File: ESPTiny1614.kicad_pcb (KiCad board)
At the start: 2 copper layers, 33 x 23.9 mm, 22 parts, among them J1 Conn_01x10_Male, J2 Conn_01x10_Male, J3 Conn_01x04_Male, U1 ESP-01v090, U2 ATtiny1614-SS, U3 MCP1700-3302E_TO92

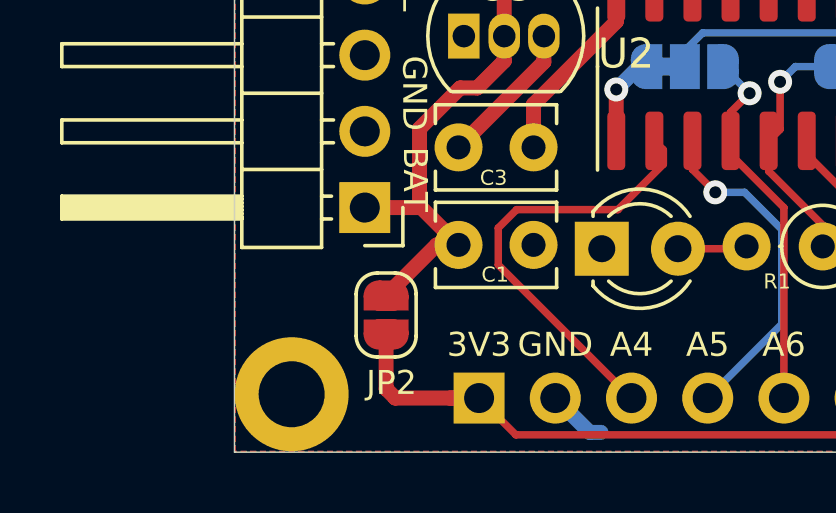
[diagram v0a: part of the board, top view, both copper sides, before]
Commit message: Change solder jumper footprint with thermal insulation
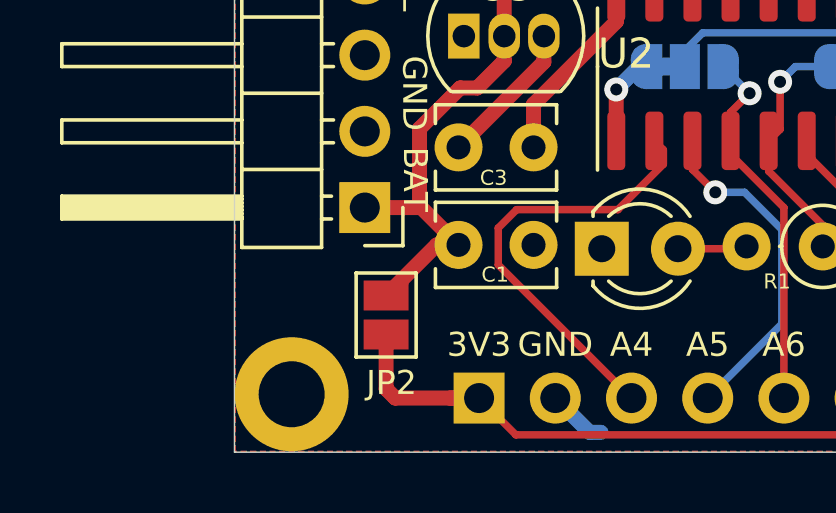
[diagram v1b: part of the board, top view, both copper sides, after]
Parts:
- JP2: footprint Jumper:SolderJumper-2_P1.3mm_Open_RoundedPad1.0x1.5mm -> Jumper:SolderJumper-2_P1.3mm_Open_Pad1.0x1.5mm

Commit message: Fix RST to A1
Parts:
- moved JP1 2.18 mm to (61.7, 51.6)
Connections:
- JP1 pad 1: /A7 -> /A1
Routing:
- net /A1: track 7.66 -> 14.8 mm, vias 0 -> 1
- net /RST: track 17.4 -> 15.2 mm
- net /A7: track 13.8 -> 12.0 mm

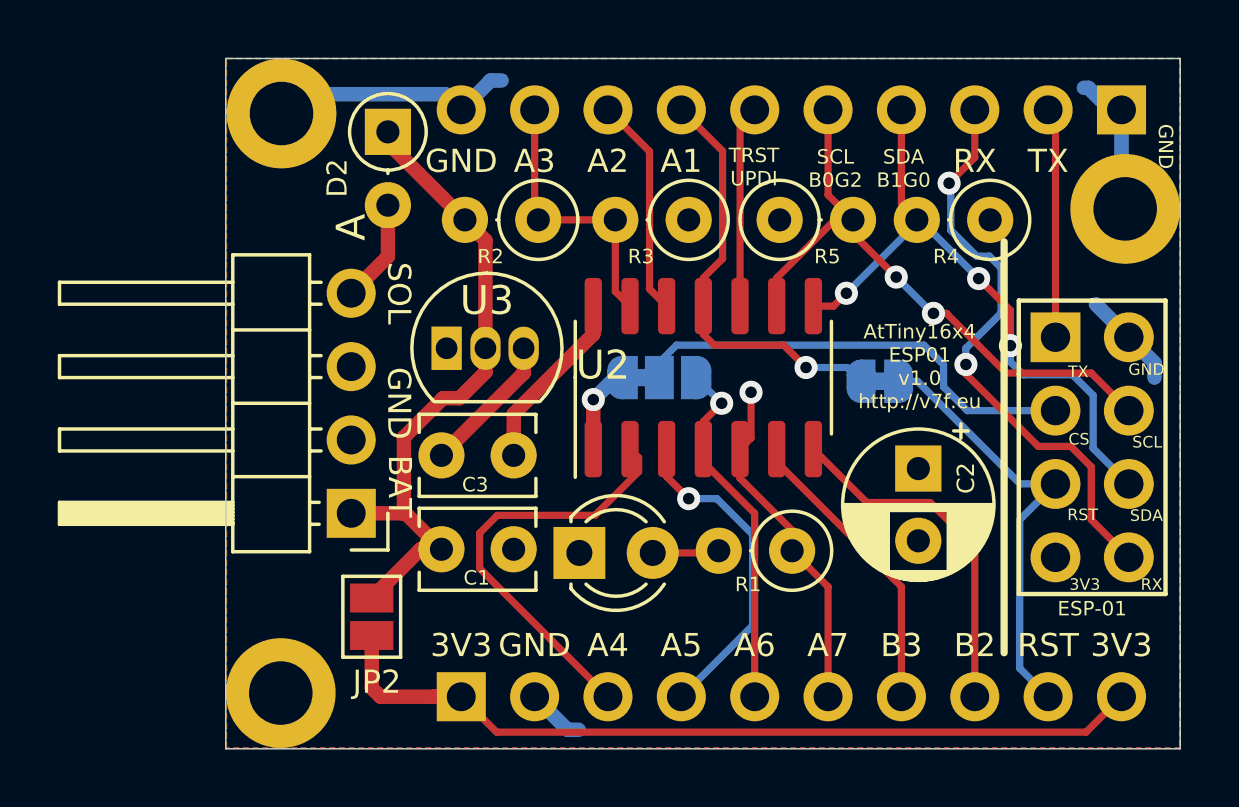
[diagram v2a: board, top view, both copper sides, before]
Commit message: Fix RST to B3
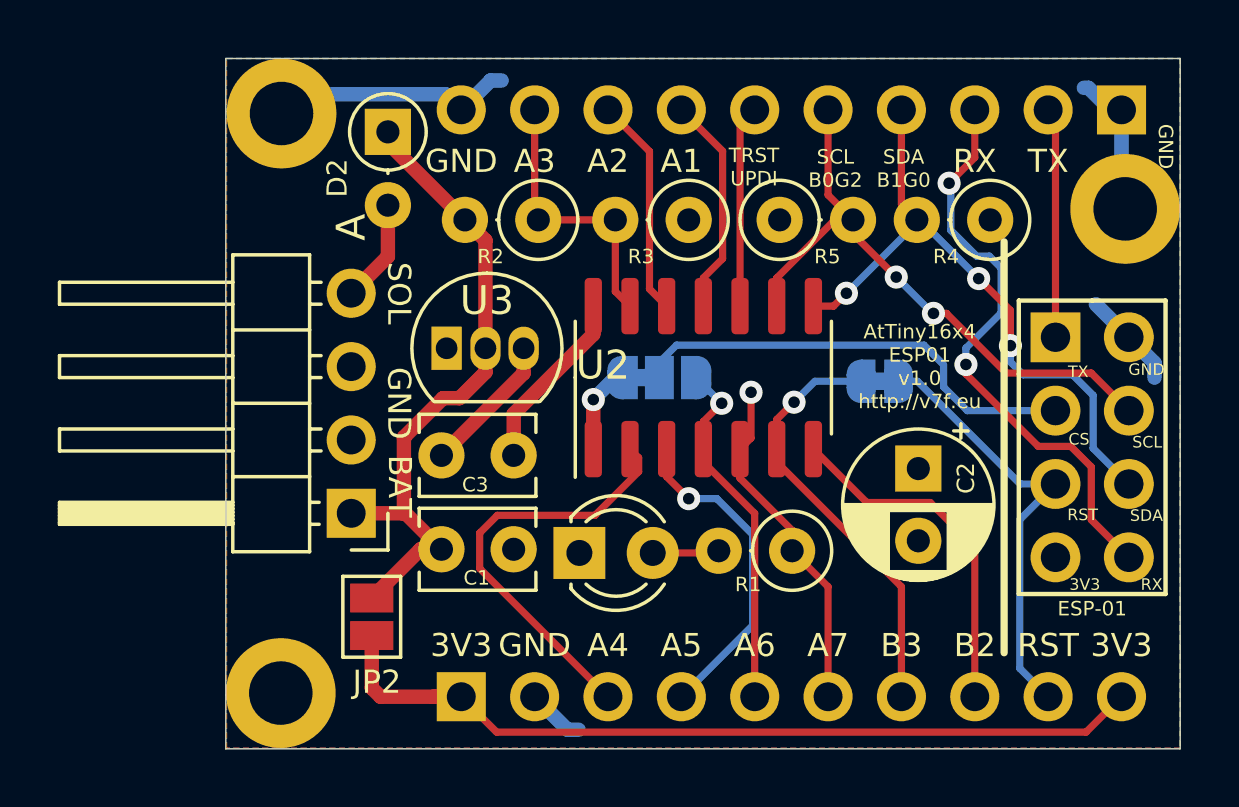
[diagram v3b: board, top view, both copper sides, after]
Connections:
- JP1 pad 1: /A1 -> /B3
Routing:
- net /A1: track 14.8 -> 7.66 mm, vias 1 -> 0
- net /B3: track 10.4 -> 14.9 mm, vias 0 -> 1
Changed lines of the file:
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@@
     (thickness 1.6)
     (drawings 57)
-    (tracks 184)
+    (tracks 182)
     (zones 0)
     (modules 22)
@@
       ))
     (pad 1 smd custom (at -0.65 0) (size 1 0.5) (layers B.Cu B.Mask)
-      (net 15 /A1) (zone_connect 2)
+      (net 17 /B3) (zone_connect 2)
       (options (clearance outline) (anchor rect))
       (primitives
@@
   (segment (start 56.293001 43.593001) (end 56.293001 47.317999) (width 0.25) (layer F.Cu) (net 15))
   (segment (start 54.864 42.164) (end 56.293001 43.593001) (width 0.25) (layer F.Cu) (net 15) (status 10))
-  (via (at 59.182 51.08499) (size 0.8) (drill 0.4) (layers F.Cu B.Cu) (net 15))
-  (segment (start 60.60999 51.08499) (end 61.087 51.562) (width 0.25) (layer B.Cu) (net 15))
-  (segment (start 59.182 51.08499) (end 60.60999 51.08499) (width 0.25) (layer B.Cu) (net 15))
-  (segment (start 55.626 49.935) (end 55.626 48.96) (width 0.25) (layer F.Cu) (net 15))
-  (segment (start 58.40702 50.31001) (end 56.00101 50.31001) (width 0.25) (layer F.Cu) (net 15))
-  (segment (start 56.00101 50.31001) (end 55.626 49.935) (width 0.25) (layer F.Cu) (net 15))
-  (segment (start 59.182 51.08499) (end 58.40702 50.31001) (width 0.25) (layer F.Cu) (net 15))
   (segment (start 64.763806 52.578) (end 67.818 52.578) (width 0.25) (layer B.Cu) (net 16))
   (segment (start 63.942291 51.756485) (end 64.763806 52.578) (width 0.25) (layer B.Cu) (net 16))
@@
   (segment (start 62.484 58.675478) (end 58.166 54.357478) (width 0.25) (layer F.Cu) (net 17) (status 20))
   (segment (start 62.484 62.484) (end 62.484 58.675478) (width 0.25) (layer F.Cu) (net 17) (status 10))
+  (via (at 58.766682 52.286642) (size 0.8) (drill 0.4) (layers F.Cu B.Cu) (net 17))
+  (segment (start 58.166 52.887324) (end 58.766682 52.286642) (width 0.25) (layer F.Cu) (net 17))
+  (segment (start 58.166 53.91) (end 58.166 52.887324) (width 0.25) (layer F.Cu) (net 17))
+  (segment (start 59.491324 51.562) (end 61.087 51.562) (width 0.25) (layer B.Cu) (net 17))
+  (segment (start 58.766682 52.286642) (end 59.491324 51.562) (width 0.25) (layer B.Cu) (net 17))
   (segment (start 47.883199 58.043199) (end 52.324 62.484) (width 0.25) (layer F.Cu) (net 18) (status 20))
   (segment (start 51.873401 56.203599) (end 48.494199 56.203599) (width 0.25) (layer F.Cu) (net 18))

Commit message: Fix RST to B3
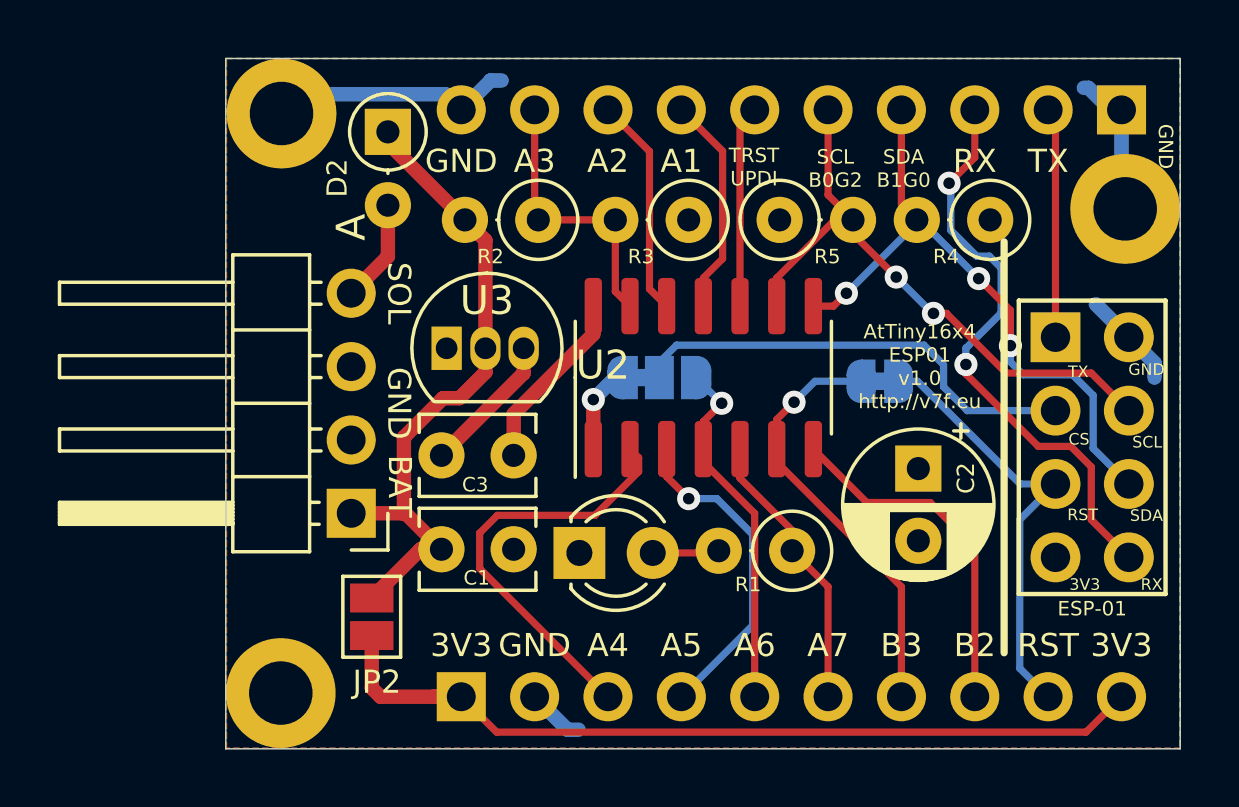
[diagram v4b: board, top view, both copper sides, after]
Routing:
- net /A7: track 12.0 -> 9.84 mm, vias 1 -> 0
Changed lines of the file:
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@@
     (thickness 1.6)
     (drawings 57)
-    (tracks 182)
+    (tracks 179)
     (zones 0)
     (modules 22)
@@
   (segment (start 59.944 58.674) (end 58.6994 57.4294) (width 0.25) (layer F.Cu) (net 8) (status 20))
   (segment (start 59.944 62.484) (end 59.944 58.674) (width 0.25) (layer F.Cu) (net 8) (status 10))
-  (via (at 57.277 51.943) (size 0.8) (drill 0.4) (layers F.Cu B.Cu) (net 8))
-  (segment (start 57.277 53.529) (end 56.896 53.91) (width 0.25) (layer F.Cu) (net 8) (status 20))
-  (segment (start 57.277 51.943) (end 57.277 53.529) (width 0.25) (layer F.Cu) (net 8))
   (segment (start 67.818 55.118) (end 66.596686 55.118) (width 0.25) (layer B.Cu) (net 9) (status 10))
   (segment (start 66.579399 56.356601) (end 67.818 55.118) (width 0.25) (layer B.Cu) (net 9) (status 20))
@@
   (segment (start 67.564 62.484) (end 66.579399 61.499399) (width 0.25) (layer B.Cu) (net 9) (status 10))
   (segment (start 63.040686 51.562) (end 66.596686 55.118) (width 0.25) (layer B.Cu) (net 9))
-  (segment (start 62.387 51.562) (end 63.040686 51.562) (width 0.25) (layer B.Cu) (net 9))
+  (segment (start 62.387 51.562) (end 63.040686 51.562) (width 0.25) (layer B.Cu) (net 9) (status 10))
   (segment (start 67.818 42.418) (end 67.564 42.164) (width 0.25) (layer F.Cu) (net 10) (status 30))
   (segment (start 67.818 50.038) (end 67.818 42.418) (width 0.25) (layer F.Cu) (net 10) (status 30))
@@
   (segment (start 56.293001 43.593001) (end 56.293001 47.317999) (width 0.25) (layer F.Cu) (net 15))
   (segment (start 54.864 42.164) (end 56.293001 43.593001) (width 0.25) (layer F.Cu) (net 15) (status 10))
-  (segment (start 64.763806 52.578) (end 67.818 52.578) (width 0.25) (layer B.Cu) (net 16))
+  (segment (start 64.763806 52.578) (end 67.818 52.578) (width 0.25) (layer B.Cu) (net 16) (status 20))
   (segment (start 63.942291 51.756485) (end 64.763806 52.578) (width 0.25) (layer B.Cu) (net 16))
   (segment (start 63.942291 50.988291) (end 63.942291 51.756485) (width 0.25) (layer B.Cu) (net 16))
   (segment (start 63.26399 50.30999) (end 63.942291 50.988291) (width 0.25) (layer B.Cu) (net 16))
   (segment (start 54.696664 50.30999) (end 63.26399 50.30999) (width 0.25) (layer B.Cu) (net 16))
-  (segment (start 54.102 50.904654) (end 54.696664 50.30999) (width 0.25) (layer B.Cu) (net 16))
-  (segment (start 54.102 51.435) (end 54.102 50.904654) (width 0.25) (layer B.Cu) (net 16))
+  (segment (start 54.102 50.904654) (end 54.696664 50.30999) (width 0.25) (layer B.Cu) (net 16) (status 10))
+  (segment (start 54.102 51.435) (end 54.102 50.904654) (width 0.25) (layer B.Cu) (net 16) (status 30))
   (segment (start 58.166 54.357478) (end 58.166 53.91) (width 0.25) (layer F.Cu) (net 17) (status 30))
   (segment (start 62.484 58.675478) (end 58.166 54.357478) (width 0.25) (layer F.Cu) (net 17) (status 20))
@@
   (via (at 58.766682 52.286642) (size 0.8) (drill 0.4) (layers F.Cu B.Cu) (net 17))
   (segment (start 58.166 52.887324) (end 58.766682 52.286642) (width 0.25) (layer F.Cu) (net 17))
-  (segment (start 58.166 53.91) (end 58.166 52.887324) (width 0.25) (layer F.Cu) (net 17))
-  (segment (start 59.491324 51.562) (end 61.087 51.562) (width 0.25) (layer B.Cu) (net 17))
+  (segment (start 58.166 53.91) (end 58.166 52.887324) (width 0.25) (layer F.Cu) (net 17) (status 10))
+  (segment (start 59.491324 51.562) (end 61.087 51.562) (width 0.25) (layer B.Cu) (net 17) (status 20))
   (segment (start 58.766682 52.286642) (end 59.491324 51.562) (width 0.25) (layer B.Cu) (net 17))
   (segment (start 47.883199 58.043199) (end 52.324 62.484) (width 0.25) (layer F.Cu) (net 18) (status 20))
